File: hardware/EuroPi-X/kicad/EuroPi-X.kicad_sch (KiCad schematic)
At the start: 154 parts, among them J1 Conn_01x16_Pin, J10 Thonkiconn_Mono_Jack, J11 Conn_02x08_Odd_Even, J12 Thonkiconn_Mono_Jack, J13 Thonkiconn_Mono_Jack, J14 Thonkiconn_Mono_Jack, J15 Thonkiconn_Mono_Jack, J16 Thonkiconn_Mono_Jack, J17 Thonkiconn_Mono_Jack, J18 Conn_01x30_Pin, J2 Conn_01x16_Pin, J3 Thonkiconn_Mono_Jack, J4 Thonkiconn_Mono_Jack, J5 Conn_01x16_Pin, J6 Thonkiconn_Mono_Jack, J7 Thonkiconn_Mono_Jack, J8 Conn_01x16_Pin, J9 Thonkiconn_Mono_Jack, P1 USB_C_Plug_USB2.0, P2 Potentiometer_9mm_Vertical_Li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, P3 Potentiometer_9mm_Vertical_Li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, SW1 BOOT, SW2 BOOT, U1 LM4030-4.096, U10 MCP3428, U11 L7805, U2 LM4040DBZ-2.0, U3 LM4040DBZ-10, U4 RP2040, U7 TL074, U8 TL074, U9 MCP6004, Y1 Crystal_GND2

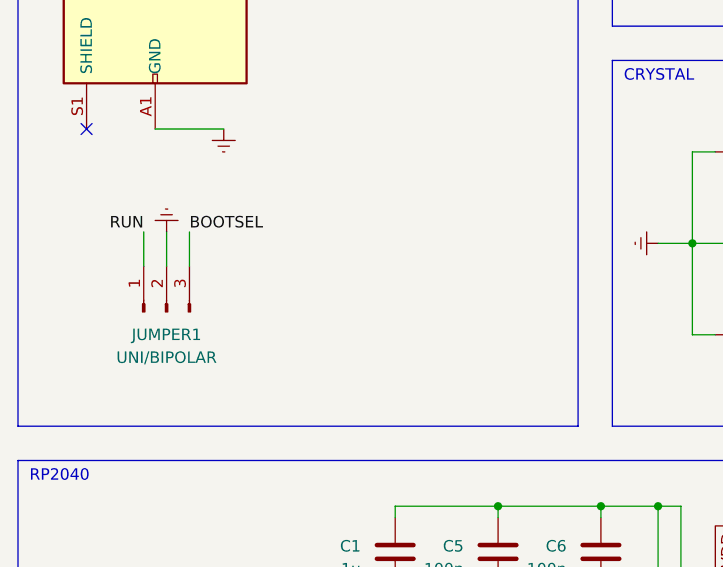
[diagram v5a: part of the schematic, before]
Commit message: create usb expander
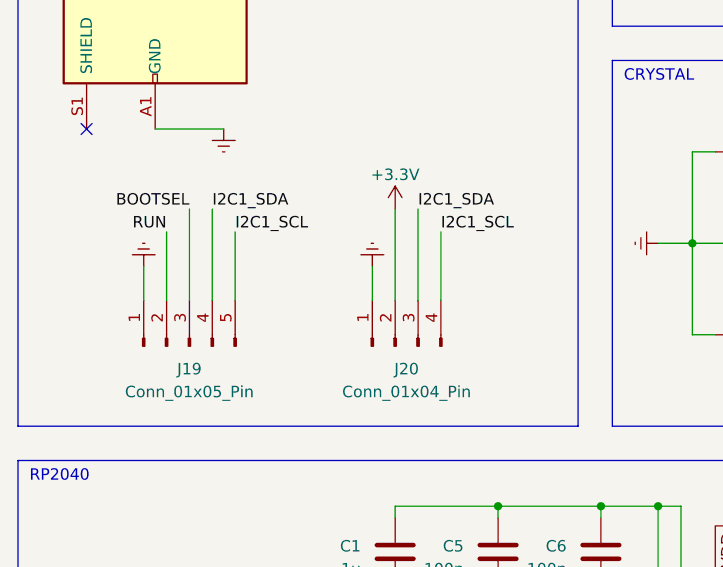
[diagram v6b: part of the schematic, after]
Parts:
- removed JUMPER1: UNI/BIPOLAR, Connector_PinHeader_2.54mm:PinHeader_1x03_P2.54mm_Vertical, symbol Connector:Conn_01x03_Pin
- added J19: Conn_01x05_Pin, Connector_PinHeader_2.54mm:PinHeader_1x05_P2.54mm_Vertical, symbol Connector:Conn_01x05_Pin
- added J20: Conn_01x04_Pin, Connector_JST:JST_SH_SM04B-SRSS-TB_1x04-1MP_P1.00mm_Horizontal, symbol Connector:Conn_01x04_Pin
- U11: footprint Package_TO_SOT_SMD:TO-252-2 -> Package_TO_SOT_SMD:TO-252-3_TabPin2
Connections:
- net +3.3V: now also J20.2 (Pin_2)
- net BOOTSEL: now also J19.3 (Pin_3)
- net Earth: now also J19.1 (Pin_1), J20.1 (Pin_1)
- net I2C1_SCL: now also J19.5 (Pin_5), J20.4 (Pin_4)
- net I2C1_SDA: now also J19.4 (Pin_4), J20.3 (Pin_3)
- net RUN: now also J19.2 (Pin_2)
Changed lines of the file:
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@@
     (stroke (width 0) (type default))
   )
-  (wire (pts (xy 38.1 81.28) (xy 38.1 85.09))
+  (wire (pts (xy 35.56 85.09) (xy 35.56 88.9))
     (stroke (width 0) (type default))
   )
@@
     (stroke (width 0) (type default))
   )
-  (wire (pts (xy 40.64 85.09) (xy 40.64 81.28))
+  (wire (pts (xy 40.64 88.9) (xy 40.64 78.74))
     (stroke (width 0) (type default))
   )
@@
     (stroke (width 0) (type default))
   )
+  (wire (pts (xy 63.5 78.74) (xy 63.5 88.9))
+    (stroke (width 0) (type default))
+  )
   (wire (pts (xy 241.3 325.12) (xy 242.57 325.12))
     (stroke (width 0) (type default))
@@
     (stroke (width 0) (type default))
   )
+  (wire (pts (xy 45.72 81.28) (xy 45.72 88.9))
+    (stroke (width 0) (type default))
+  )
   (wire (pts (xy 232.41 38.1) (xy 232.41 40.64))
     (stroke (width 0) (type default))
@@
     (stroke (width 0) (type default))
   )
+  (wire (pts (xy 68.58 81.28) (xy 68.58 88.9))
+    (stroke (width 0) (type default))
+  )
   (wire (pts (xy 257.81 176.53) (xy 265.43 176.53))
     (stroke (width 0) (type default))
@@
     (stroke (width 0) (type default))
   )
+  (wire (pts (xy 43.18 78.74) (xy 43.18 88.9))
+    (stroke (width 0) (type default))
+  )
   (wire (pts (xy 368.3 148.59) (xy 373.38 148.59))
     (stroke (width 0) (type default))
@@
     (stroke (width 0) (type default))
   )
+  (wire (pts (xy 66.04 78.74) (xy 66.04 88.9))
+    (stroke (width 0) (type default))
+  )
   (wire (pts (xy 447.04 205.74) (xy 448.31 205.74))
     (stroke (width 0) (type default))
@@
     (stroke (width 0) (type default))
   )
+  (wire (pts (xy 60.96 85.09) (xy 60.96 88.9))
+    (stroke (width 0) (type default))
+  )
   (wire (pts (xy 128.27 163.83) (xy 123.19 163.83))
     (stroke (width 0) (type default))
@@
     (stroke (width 0) (type default))
   )
-  (wire (pts (xy 35.56 85.09) (xy 35.56 81.28))
+  (wire (pts (xy 38.1 88.9) (xy 38.1 81.28))
     (stroke (width 0) (type default))
   )
@@
     (effects (font (size 1.27 1.27)) (justify right bottom))
   )
-  (label "RUN" (at 35.56 81.28 180) (fields_autoplaced)
+  (label "RUN" (at 38.1 81.28 180) (fields_autoplaced)
     (effects (font (size 1.27 1.27)) (justify right bottom))
   )
@@
     (effects (font (size 1.27 1.27)) (justify right bottom))
   )
-  (label "BOOTSEL" (at 40.64 81.28 0) (fields_autoplaced)
-    (effects (font (size 1.27 1.27)) (justify left bottom))
+  (label "BOOTSEL" (at 40.64 78.74 180) (fields_autoplaced)
+    (effects (font (size 1.27 1.27)) (justify right bottom))
   )
   (label "CV_OUTPUT_4_FRONT" (at 515.62 265.43 90) (fields_autoplaced)
@@
     (effects (font (size 1.27 1.27)) (justify left bottom))
   )
+  (label "I2C1_SDA" (at 66.04 78.74 0) (fields_autoplaced)
+    (effects (font (size 1.27 1.27)) (justify left bottom))
+  )
   (label "DAC_1_OUTC" (at 76.2 255.27 0) (fields_autoplaced)
     (effects (font (size 1.27 1.27)) (justify left bottom))
@@
     (effects (font (size 1.27 1.27)) (justify left bottom))
   )
+  (label "I2C1_SCL" (at 68.58 81.28 0) (fields_autoplaced)
+    (effects (font (size 1.27 1.27)) (justify left bottom))
+  )
   (label "-2.048VREF" (at 72.39 321.31 0) (fields_autoplaced)
     (effects (font (size 1.27 1.27)) (justify left bottom))
@@
     (effects (font (size 1.27 1.27)) (justify left bottom))
   )
+  (label "I2C1_SDA" (at 43.18 78.74 0) (fields_autoplaced)
+    (effects (font (size 1.27 1.27)) (justify left bottom))
+  )
   (label "-10VREF" (at 227.33 176.53 180) (fields_autoplaced)
     (effects (font (size 1.27 1.27)) (justify right bottom))
@@
     (effects (font (size 1.27 1.27)) (justify left bottom))
   )
+  (label "I2C1_SCL" (at 45.72 81.28 0) (fields_autoplaced)
+    (effects (font (size 1.27 1.27)) (justify left bottom))
+  )
   (label "ADC_INPUT_3" (at 410.21 132.08 180) (fields_autoplaced)
     (effects (font (size 1.27 1.27)) (justify right bottom))
@@
     )
   )
-  (symbol (lib_id "Connector:Conn_01x03_Pin") (at 38.1 90.17 90) (unit 1)
-    (in_bom yes) (on_board yes) (dnp no) (fields_autoplaced)
-    (property "Reference" "JUMPER1" (at 38.1 92.71 90)
-      (effects (font (size 1.27 1.27)))
-    )
-    (property "Value" "UNI/BIPOLAR" (at 38.1 95.25 90)
-      (effects (font (size 1.27 1.27)))
-    )
-    (property "Footprint" "Connector_PinHeader_2.54mm:PinHeader_1x03_P2.54mm_Vertical" (at 38.1 90.17 0)
-      (effects (font (size 1.27 1.27)) hide)
-    )
-    (property "Datasheet" "~" (at 38.1 90.17 0)
-      (effects (font (size 1.27 1.27)) hide)
-    )
-    (pin "1")
-    (pin "2")
-    (pin "3")
-    (instances
-      (project "EuroPi-X"
-        (path "/a1be51f2-61d0-4240-8665-f31cc7b044f7"
-          (reference "JUMPER1") (unit 1)
-        )
-      )
-    )
-  )
   (symbol (lib_id "Device:C") (at 232.41 45.72 0) (unit 1)
     (in_bom yes) (on_board yes) (dnp no)
@@
     )
   )
+  (symbol (lib_id "power:Earth") (at 60.96 85.09 180) (unit 1)
+    (in_bom yes) (on_board yes) (dnp no) (fields_autoplaced)
+    (property "Reference" "#PWR067" (at 60.96 78.74 0)
+      (effects (font (size 1.27 1.27)) hide)
+    )
+    (property "Value" "Earth" (at 60.96 81.28 0)
+      (effects (font (size 1.27 1.27)) hide)
+    )
+    (property "Footprint" "" (at 60.96 85.09 0)
+      (effects (font (size 1.27 1.27)) hide)
+    )
+    (property "Datasheet" "~" (at 60.96 85.09 0)
+      (effects (font (size 1.27 1.27)) hide)
+    )
+    (pin "1")
+    (instances
+      (project "EuroPi-X"
+        (path "/a1be51f2-61d0-4240-8665-f31cc7b044f7"
+          (reference "#PWR067") (unit 1)
+        )
+      )
+      (project "usb-hub"
+        (path "/fd314b15-8a64-4cdc-b5d9-7360b63466b4"
+          (reference "#PWR015") (unit 1)
+        )
+      )
+    )
+  )
   (symbol (lib_id "Eurorack:Thonkiconn_Mono_Jack") (at 435.61 320.04 0) (mirror y) (unit 1)
     (in_bom yes) (on_board yes) (dnp no)
@@
       (effects (font (size 1.27 1.27)))
     )
-    (property "Footprint" "Package_TO_SOT_SMD:TO-252-2" (at 454.025 398.78 0)
+    (property "Footprint" "Package_TO_SOT_SMD:TO-252-3_TabPin2" (at 454.025 398.78 0)
       (effects (font (size 1.27 1.27) italic) (justify left) hide)
     )
@@
     )
   )
+  (symbol (lib_id "Connector:Conn_01x05_Pin") (at 40.64 93.98 90) (unit 1)
+    (in_bom yes) (on_board yes) (dnp no) (fields_autoplaced)
+    (property "Reference" "J19" (at 40.64 96.52 90)
+      (effects (font (size 1.27 1.27)))
+    )
+    (property "Value" "Conn_01x05_Pin" (at 40.64 99.06 90)
+      (effects (font (size 1.27 1.27)))
+    )
+    (property "Footprint" "Connector_PinHeader_2.54mm:PinHeader_1x05_P2.54mm_Vertical" (at 40.64 93.98 0)
+      (effects (font (size 1.27 1.27)) hide)
+    )
+    (property "Datasheet" "~" (at 40.64 93.98 0)
+      (effects (font (size 1.27 1.27)) hide)
+    )
+    (pin "1")
+    (pin "2")
+    (pin "3")
+    (pin "4")
+    (pin "5")
+    (instances
+      (project "EuroPi-X"
+        (path "/a1be51f2-61d0-4240-8665-f31cc7b044f7"
+          (reference "J19") (unit 1)
+        )
+      )
+    )
+  )
   (symbol (lib_id "Eurorack:Thonkiconn_Mono_Jack") (at 252.73 270.51 0) (mirror y) (unit 1)
     (in_bom yes) (on_board yes) (dnp no)
@@
     )
   )
-  (symbol (lib_id "power:Earth") (at 38.1 81.28 180) (unit 1)
+  (symbol (lib_id "power:Earth") (at 35.56 85.09 180) (unit 1)
     (in_bom yes) (on_board yes) (dnp no) (fields_autoplaced)
-    (property "Reference" "#PWR04" (at 38.1 74.93 0)
+    (property "Reference" "#PWR04" (at 35.56 78.74 0)
       (effects (font (size 1.27 1.27)) hide)
     )
-    (property "Value" "Earth" (at 38.1 77.47 0)
+    (property "Value" "Earth" (at 35.56 81.28 0)
       (effects (font (size 1.27 1.27)) hide)
     )
-    (property "Footprint" "" (at 38.1 81.28 0)
+    (property "Footprint" "" (at 35.56 85.09 0)
       (effects (font (size 1.27 1.27)) hide)
     )
-    (property "Datasheet" "~" (at 38.1 81.28 0)
+    (property "Datasheet" "~" (at 35.56 85.09 0)
       (effects (font (size 1.27 1.27)) hide)
     )
@@
     )
   )
+  (symbol (lib_id "power:+3.3V") (at 63.5 78.74 0) (unit 1)
+    (in_bom yes) (on_board yes) (dnp no) (fields_autoplaced)
+    (property "Reference" "#PWR078" (at 63.5 82.55 0)
+      (effects (font (size 1.27 1.27)) hide)
+    )
+    (property "Value" "+3.3V" (at 63.5 74.93 0)
+      (effects (font (size 1.27 1.27)))
+    )
+    (property "Footprint" "" (at 63.5 78.74 0)
+      (effects (font (size 1.27 1.27)) hide)
+    )
+    (property "Datasheet" "" (at 63.5 78.74 0)
+      (effects (font (size 1.27 1.27)) hide)
+    )
+    (pin "1")
+    (instances
+      (project "EuroPi-X"
+        (path "/a1be51f2-61d0-4240-8665-f31cc7b044f7"
+          (reference "#PWR078") (unit 1)
+        )
+      )
+    )
+  )
   (symbol (lib_id "Device:R") (at 283.21 273.05 270) (unit 1)
     (in_bom yes) (on_board yes) (dnp no)
@@
         )
       )
+    )
+  )
+  (symbol (lib_id "Connector:Conn_01x04_Pin") (at 63.5 93.98 90) (unit 1)
+    (in_bom yes) (on_board yes) (dnp no) (fields_autoplaced)
+    (property "Reference" "J20" (at 64.77 96.52 90)
+      (effects (font (size 1.27 1.27)))
+    )
+    (property "Value" "Conn_01x04_Pin" (at 64.77 99.06 90)
+      (effects (font (size 1.27 1.27)))
+    )
+    (property "Footprint" "Connector_JST:JST_SH_SM04B-SRSS-TB_1x04-1MP_P1.00mm_Horizontal" (at 63.5 93.98 0)
+      (effects (font (size 1.27 1.27)) hide)
+    )
+    (property "Datasheet" "~" (at 63.5 93.98 0)
+      (effects (font (size 1.27 1.27)) hide)
+    )
+    (pin "1")
+    (pin "2")
+    (pin "3")
+    (pin "4")
+    (instances
+      (project "EuroPi-X"
+        (path "/a1be51f2-61d0-4240-8665-f31cc7b044f7"
+          (reference "J20") (unit 1)
+        )
+      )

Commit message: save
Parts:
- removed JUMPER3: UNI/BIPOLAR, Connector_PinHeader_2.54mm:PinHeader_1x03_P2.54mm_Vertical, symbol Connector:Conn_01x03_Pin
- added JUMPER1: UNI/BIPOLAR, Connector_PinHeader_2.54mm:PinHeader_1x03_P2.54mm_Vertical, symbol Connector:Conn_01x03_Pin
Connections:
- net +12V: now also JUMPER1.3 (Pin_3)
- net 5VREG_INPUT: now also JUMPER1.2 (Pin_2)
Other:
- note removed: "Jumper sets internal 5V regulator"
- moved on the sheet: C2, C3, C34, C4, J18, R1, R10, R11, R2, R3, R55, TP4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

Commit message: save
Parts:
- removed J19: Conn_01x05_Pin, Connector_PinHeader_2.54mm:PinHeader_1x05_P2.54mm_Vertical, symbol Connector:Conn_01x05_Pin
- removed TP4, TP6, TP7, TP8: TestPoint, TestPoint:TestPoint_Pad_1.0x1.0mm, symbol Connector:TestPoint
- added D6: D, Diode_SMD:D_0402_1005Metric, symbol Device:D
- added J19, J21: Conn_01x04_Pin, Connector_PinHeader_2.54mm:PinHeader_1x04_P2.54mm_Vertical, symbol Connector:Conn_01x04_Pin
- added Q1: BSS138, Package_TO_SOT_SMD:SOT-23, symbol Transistor_FET:BSS138
- added R58: 5K6, Resistor_SMD:R_0402_1005Metric, symbol Device:R
- added R59: 10K, Resistor_SMD:R_0402_1005Metric, symbol Device:R
- C1, C10, C15, C16, C2, C3, C4, C7: JLCPCB PART# (none) -> C52923
- C13, C14, C17, C18, C21, C22, C23, C24, C27, C31, C34, C35, C36, C5, C6: JLCPCB PART# (none) -> C1525
- C25, C26, C28: JLCPCB PART# (none) -> C15850
- C8, C9: JLCPCB PART# (none) -> C32949
- D1, D2, D5: value ${SIM.PARAMS} -> type="D" model="DIODE" lib=""; JLCPCB PART# (none) -> C95872
- DAC1, DAC2: JLCPCB PART# (none) -> C108207
- R10, R8, R9: JLCPCB PART# (none) -> C25744
- R11, R18, R19, R33, R34, R47, R48, R56, R57: JLCPCB PART# (none) -> C11702
- R12, R13, R14, R15, R20, R21, R22, R23, R27, R28, R29, R30, R35, R36, R37, R38, R41, R42, R43, R44, R49, R50, R51, R52: JLCPCB PART# (none) -> C25741
- R16, R17, R31, R32, R45, R46, R53, R54: JLCPCB PART# (none) -> C170277
- R25, R26, R39, R40: JLCPCB PART# (none) -> C25756
- R6, R7: value 22 -> 10K; JLCPCB PART# C25092 -> C25744
- SW1: value BOOT -> B1
- SW2: value BOOT -> B2
- U10: JLCPCB PART# (none) -> C560166
- U4: JLCPCB PART# (none) -> C2040
- Y1: footprint Crystal:Crystal_SMD_7050-4Pin_7.0x5.0mm -> Crystal:Crystal_SMD_3225-4Pin_3.2x2.5mm; JLCPCB PART# (none) -> C9002
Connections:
- net VREG_IN is gone; now on net +3.3V: U4.44 (VREG_IN)
- net +3.3V: now also R6.2, U4.8 (GPIO6), J19.2 (Pin_2), J21.2 (Pin_2), Q1.1 (G); no longer U4.2 (GPIO0)
- net +5V: now also R7.2, D6.1 (K); no longer P1.A4 (VBUS), P1.A9 (VBUS), P1.B4 (VBUS), P1.B9 (VBUS)
- net BOOTSEL: now also J19.4 (Pin_4)
- net BUTTON_1: now also U4.6 (GPIO4); no longer U4.13 (GPIO10)
- net BUTTON_2: now also U4.7 (GPIO5); no longer U4.12 (GPIO9)
- net Earth: now also U4.11 (GPIO8), U4.12 (GPIO9), U4.9 (GPIO7), U7.10 (+), U7.12 (+), U7.3 (+), U7.5 (+), U8.10 (+), U8.12 (+), U8.3 (+), U8.5 (+), J19.1 (Pin_1), J21.1 (Pin_1), R59.1; no longer U4.3 (GPIO1), U7.13 (-), U7.2 (-), U7.6 (-), U7.9 (-), U8.13 (-), U8.2 (-), U8.6 (-), U8.9 (-)
- net I2C0_SCL: now also U4.3 (GPIO1); no longer U4.7 (GPIO5)
- net I2C0_SDA: now also U4.2 (GPIO0); no longer U4.6 (GPIO4)
- net I2C1_SCL: now also U4.5 (GPIO3), J21.4 (Pin_4); no longer U4.9 (GPIO7)
- net I2C1_SDA: now also U4.4 (GPIO2), J21.3 (Pin_3); no longer U4.8 (GPIO6)
- net INPUT_DETECT: now also U4.18 (GPIO15); no longer U4.5 (GPIO3)
- net OLED_CLK: now also U4.13 (GPIO10); no longer U4.17 (GPIO14)
- net OUTPUT_MODE: now also U4.15 (GPIO12); no longer U4.4 (GPIO2)
- net RUN: now also J19.3 (Pin_3)
- net USB_DN: now also P1.A7 (D-); no longer R6.2
- net USB_DP: now also P1.A6 (D+); no longer R7.2
- net at C11.1, R12.1, R13.1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: now also U7.13 (-); no longer U7.12 (+)
- net NEOPIXEL_DATA_5V: now reaches R7.1
- net NEOPIXEL_DATA_5V: now also J8.11 (Pin_11), Q1.3 (D); no longer P1.A6 (D+)
- net at C20.1, R29.1, R30.1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: now also U8.2 (-); no longer U8.3 (+)
- net at C12.1, R14.1, R15.1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: now also U8.13 (-); no longer U8.12 (+)
- net at C33.1, R51.1, R52.1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: now also U8.9 (-); no longer U8.10 (+)
- net at C32.1, R49.1, R50.1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: now also U7.9 (-); no longer U7.10 (+)
- net NEOPIXEL_DATA_3V3: now reaches R6.1
- net NEOPIXEL_DATA_3V3: now also U4.17 (GPIO14), Q1.2 (S); no longer P1.A7 (D-)
- net at C19.1, R27.1, R28.1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: now also U7.2 (-); no longer U7.3 (+)
- net at C29.1, R41.1, R42.1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: now also U7.6 (-); no longer U7.5 (+)
- net at C30.1, R43.1, R44.1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: now also U8.6 (-); no longer U8.5 (+)
- net ADC_AVDD renamed ADC_VDD
- removed net NEOPIXEL_DATA: J8.11 (Pin_11), U4.11 (GPIO8)
- new net USB_DETECT: R58.1, R59.2
- new net VBUS: D6.2 (A), P1.A4 (VBUS), P1.A9 (VBUS), P1.B4 (VBUS), P1.B9 (VBUS), R58.2
- no-connect marks 18 -> 30
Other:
- note added: "+5V REGULATOR"
- note added: "2.54mm connector for i2c"
- note added: "DAC_OFFSET is added to the signal to determine if it is unipolar or bipolar."
- note added: "DAC_OFFSET is voltage divided down to 1.024V in bipolar mode, below the ~1.8V threshold for a GPIO to be read as 'high', or 2.048V in unipolar mode, above the threshold. Thus OUTPUT_MODE can be used by the software to determine if the module is in unipolar or bipolar mode without requiring an extra jumper"
- note added: "EURORACK POWER"
- note added: "EXPANDERS"
- note added: "Expander for buttons (reset and bootsel)"
- note added: "GP6 - GP9 are used as a binary signal that represents the EuroPi hardware type 0000 - EuroPi 0001 - EuroPi X 0010 - Undetermined etc"
- note added: "In bipolar mode, the signal is offset by -2.048V, resulting in a signal from -2.048V to +2.048V It is then inverted and amplified by 2.7x resulting in a signal from +5.53VV to -5.53V (the clipping to ±5V and flipping of direction happens in software)"
- note added: "STEMMA QT connector for i2c"
- note added: "Schottky diode prevents reverse powering of the USB connection from the module's internal 5V rail"
- note added: "The INPUT_DETECT signal is clamped using two diodes to prevent it from going above 3.3V or below Ground. This is because when a jack is plugged in, the tip of the jack (which may be in the range of ±10V) will briefly contact the switched pin, so the RP2040 pin must be protected"
- note added: "The Neopixel LEDs are serial controlled, meaning only a single pin of the RP2040 is connected to the first LED, and the remaning LEDs are connected in series. They are powered by 5V, but the RP2040 signal is only 3.3V, so a level shifter is used."
- note added: "The capacitor is used to prevent ringing"
- note added: "The flash chip is pin compatible with other sizes; the 64 in the part number can be exchanged for other values for different amounts of flash storage W25Q16JVXGIQ - 2 Megabytes (This is used on the Raspberry Pi Pico) W25Q32JVXGIQ - 4 Megabytes W25Q64JVXGIQ - 8 Megabytes (This is used on the EuroPi X) W25Q128JVXGIQ - 16 Megabytes"
- note added: "The incoming signal from the DAC is from 0 to 4.096V In unipolar mode, the signal is offset by -4.096V, resulting in a signal from -4.096V to 0V It is then inverted and amplified by 2.7x resulting in a signal from 11.05V to 0V (the clipping to +10V and flipping of direction happens in software)"
- note added: "The incoming signal is in the range ±10V It has the offset of -10V added to it, resulting in a range of -20V to 0V It is then inverted and attenuated by 0.15x resulting in a range of +3V to 0V, which is a safe range to feed into the +3.3V tolerant ADC input. If a signal did go above the range of ±10V, it would still be clamped to the rails of the op-amp, which are 0V and +3.3V, so the ADC input i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"
- note added: "The user can set whether to use the internal +5V regulator by setting the jumper to either power the regulator with +12V or not"
- note added: "VBUS is voltage divided to 3.3v (3.205V) and detected by USB_DETECT to allow code to determine if USB power is active"
- note added: "i2c connectors use i2c bus 1"
- note removed: "OUTPUT_MODE is high when mode is unipolar"
- moved on the sheet: C1, C10, C11, C12, C13, C14, C15, C16, C17, C18, C19, C2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
